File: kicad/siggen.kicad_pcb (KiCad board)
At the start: 4 copper layers, 39 x 60 mm, 100 parts, among them J1 Conn_Coaxial, J2 USB_C_Receptacle_USB2.0, Q1 BC857, Q2 BC847, Q3 BC857, U1 AD9954, U2 OPA859xDSG, U3 MCP2210x-SS, U4 AP62201-SOT563, U5 AP62201-SOT563, U6 TLV71x, U7 TLV71x, X1 ASE-xxxMHz, Y1 CSTNE12M0GH5L000R0

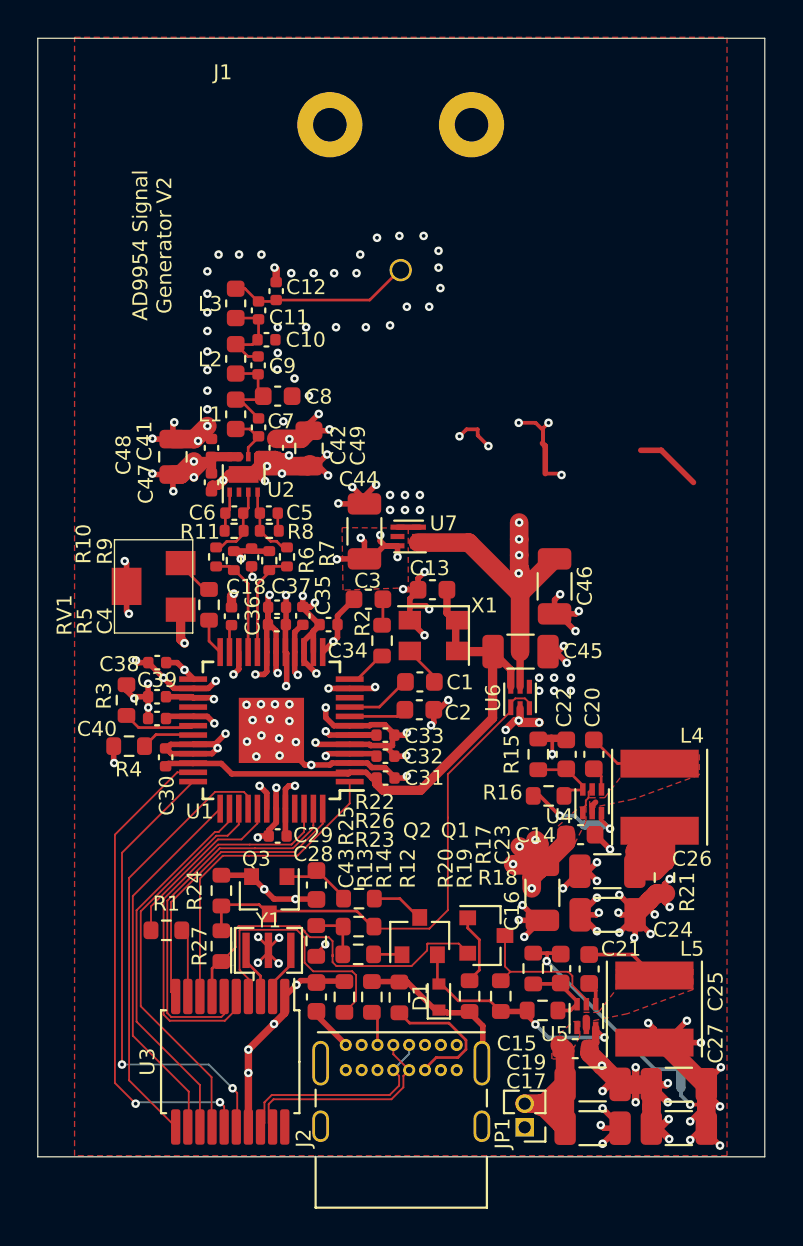
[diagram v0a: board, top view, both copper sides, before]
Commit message: Added output buffer; power LED
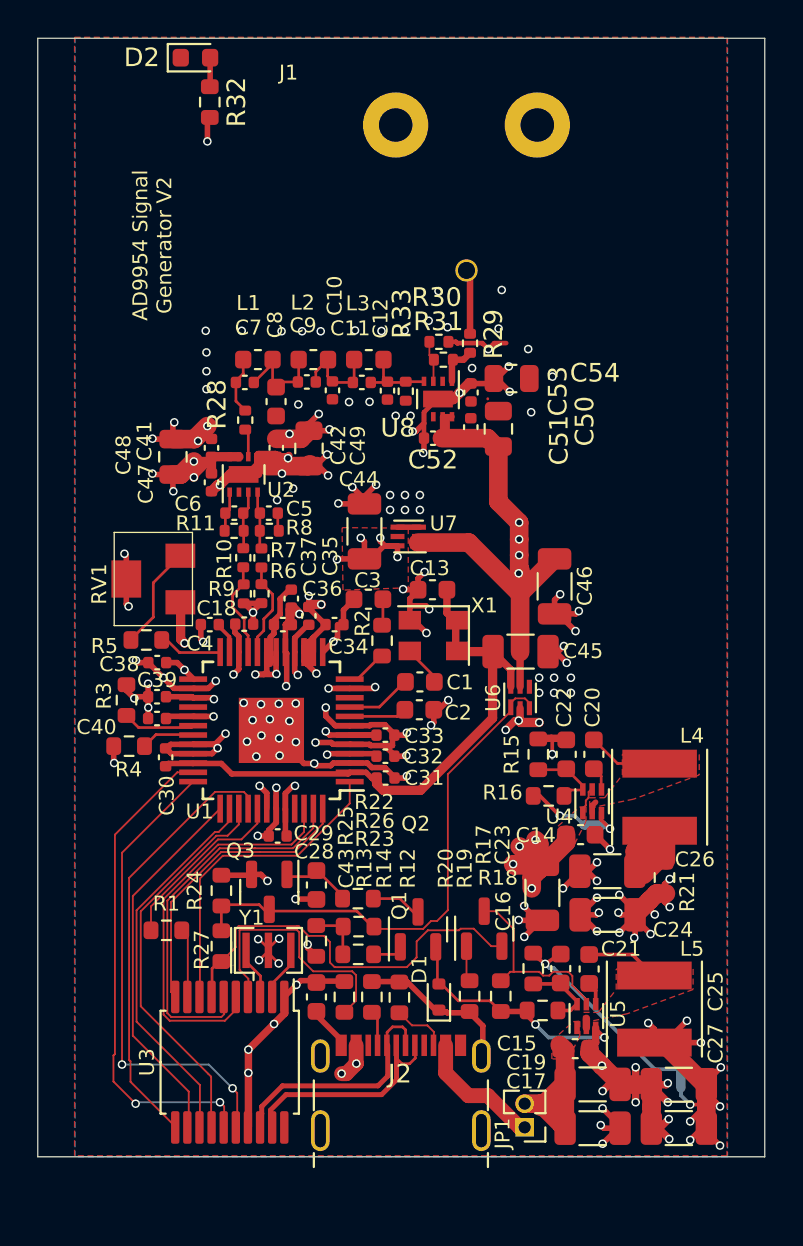
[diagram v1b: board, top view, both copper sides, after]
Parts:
- added C50: 1u, Capacitor_SMD:C_0805_2012Metric, F.Cu at (122.7, 121.0)
- added C51: 100n, Capacitor_SMD:C_0402_1005Metric, F.Cu at (121.2, 120.9)
- added C52: 100n, Capacitor_SMD:C_0402_1005Metric, F.Cu at (119.2, 121.5)
- added C53: 100n, Capacitor_SMD:C_0402_1005Metric, F.Cu at (121.2, 119.0)
- added C54: 1u, Capacitor_SMD:C_0805_2012Metric, F.Cu at (123.4, 118.2)
- added D2: LED, LED_SMD:LED_0603_1608Metric, F.Cu at (106.5, 101.0)
- added R28: 0, Resistor_SMD:R_0402_1005Metric, F.Cu at (109.1, 120.5)
- added R29: 0, Resistor_SMD:R_0402_1005Metric, F.Cu at (121.2, 116.4)
- added R30: 50, Resistor_SMD:R_0402_1005Metric, F.Cu at (119.5, 116.3)
- added R31: 50, Resistor_SMD:R_0402_1005Metric, F.Cu at (119.8, 117.2)
- added R32: 1k, Resistor_SMD:R_0603_1608Metric, F.Cu at (107.2, 103.4)
- added R33: 50, Resistor_SMD:R_0402_1005Metric, F.Cu at (117.7, 118.9)
- added U8: OPA859xDSG, Package_SON:WSON-8-1EP_2x2mm_P0.5mm_EP0.9x1.6mm, F.Cu at (119.5, 119.3)
- C5, C6: value 5.09p -> 7.3p
- J2: footprint proj_footprints:USB_C_Receptacle_GCT_USB4085_smaller_holes -> proj_footprints:USB_C_Receptacle_Molex_2171790001_16P_TopMnt_Horizontal
- R10, R7: value 142 -> 82
- R11, R8: value 220 -> 150
- R6, R9: value 120 -> 82
- moved C12 8.01 mm to (116.8, 118.9), turned to -90 degrees
- moved L3 7.75 mm to (115.8, 117.2), turned to 180 degrees
- moved C11 6.75 mm to (115.4, 118.5), turned to 180 degrees
- moved J2 4.74 mm to (117.5, 157.7)
- moved C10 4.46 mm to (113.8, 118.9), turned to -90 degrees
- moved L2 4.17 mm to (112.8, 117.2), turned to 180 degrees
- moved R5 3.86 mm to (103.8, 132.3), turned to 0 degrees
- moved C18 3.60 mm to (109.1, 131.4), turned to 0 degrees
- moved J1 3.53 mm to (121.0, 104.7)
- moved L1 3.17 mm to (109.8, 117.2), turned to 180 degrees
- moved C9 2.76 mm to (112.4, 118.4), turned to 180 degrees
- moved C7 2.52 mm to (109.1, 118.5), turned to 180 degrees
- moved R9 1.86 mm to (109.0, 129.8), turned to -90 degrees
- moved R6 1.82 mm to (110.0, 129.8), turned to -90 degrees
- moved R10 1.46 mm to (109.0, 127.9)
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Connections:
- C11 pad 1: /dds_analog/OUT_50 -> Net-(U8-+)
- C12 pad 1: /dds_analog/OUT_50 -> Net-(U8-+)
- J2 pad A8: Net-(J2-PadA8) -> unconnected-(J2-SBU1-PadA8)
- J2 pad B8: Net-(J2-PadB8) -> unconnected-(J2-SBU2-PadB8)
- L3 pad 1: /dds_analog/OUT_50 -> Net-(U8-+)
- U1 pad 10: Net-(U1-Pad10) -> unconnected-(U1-CRYSTAL_OUT-Pad10)
- U1 pad 28: Net-(U1-Pad28) -> unconnected-(U1-COMP_OUT-Pad28)
- U1 pad 45: Net-(U1-Pad45) -> unconnected-(U1-SYNC_CLK-Pad45)
- U2 pad 2: Net-(U2-Pad2) -> unconnected-(U2-NC-Pad2)
- U2 pad 6: Net-(C7-Pad2) -> Net-(R28-Pad1)
- U7 pad 5: Net-(U7-Pad5) -> unconnected-(U7-VOUT2-Pad5)
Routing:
- net +3V0: track 59.0 -> 108.3 mm, vias 9 -> 10
- net Net-(J2-VBUS-PadA4): track 0.00 -> 19.5 mm, vias 0 -> 2
- net -2V2: track 42.9 -> 51.1 mm, vias 18 -> 20
- net /dds_analog/OUT_50: track 9.83 -> 3.49 mm
- net GND: track 158.9 -> 152.9 mm, vias 143 -> 131
- net Net-(J2-CC2): track 7.34 -> 2.95 mm
- net Net-(U8-+): track 0.00 -> 4.14 mm
- net Net-(R5-Pad1): track 2.20 -> 5.66 mm
- net PWR_EN: track 19.3 -> 22.0 mm
- net Net-(Q1-C): track 8.06 -> 10.4 mm
- net Net-(U8--): track 0.00 -> 2.21 mm
- net Net-(U8-FB): track 0.00 -> 2.07 mm
- net Net-(Q1-B): track 3.86 -> 1.97 mm
- net +3V3: track 37.0 -> 35.2 mm
- net Net-(D2-A): track 0.00 -> 1.61 mm
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- added copper zone on B.Cu, net GND
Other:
- net class Default removed
- net class eurockt_diff100 removed
- net class eurockt_se50 removed
- net class jlc_diff100 removed
- net class jlc_se50 removed

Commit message: prepare for jlcpcb order (v2)
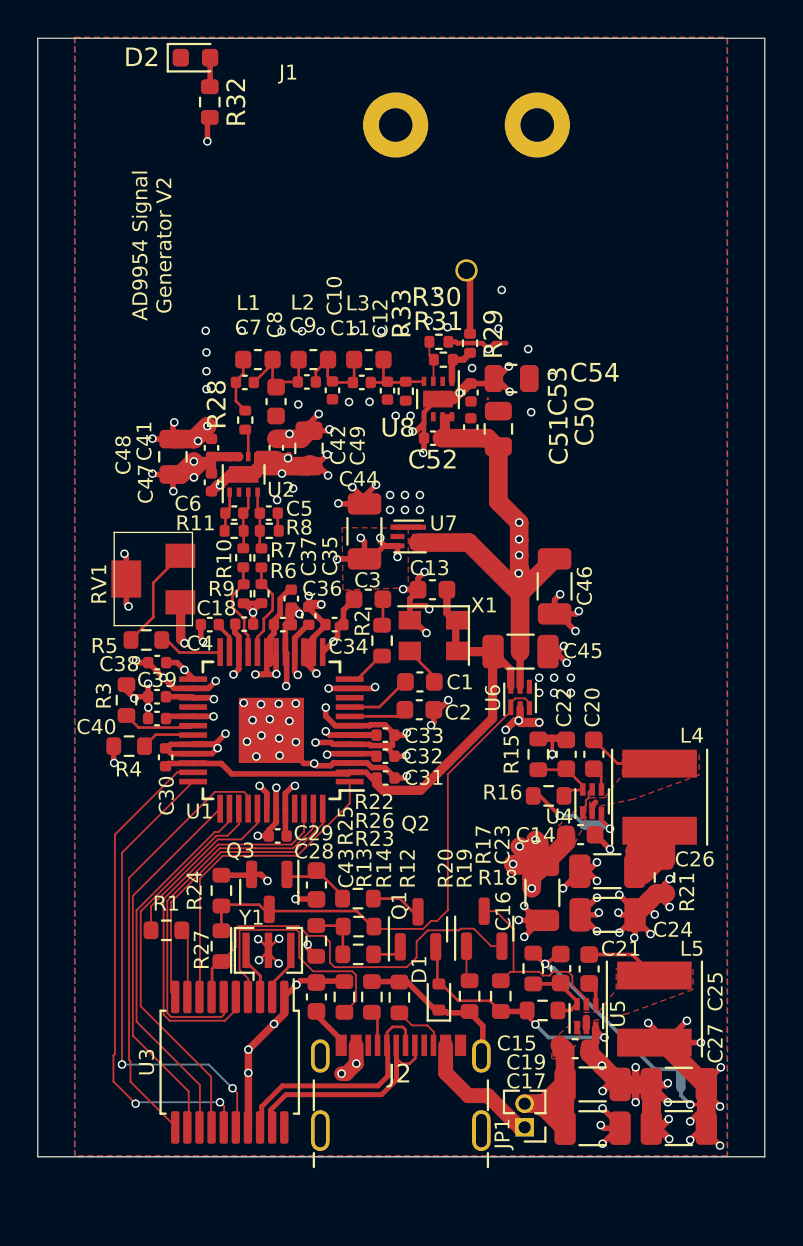
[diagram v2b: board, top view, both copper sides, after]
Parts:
- R30, R31: value 50 -> 150
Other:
- rule pad_to_mask_clearance: 0.048 -> 0
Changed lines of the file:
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@@
       (dielectric_constraints no)
     )
-    (pad_to_mask_clearance 0.048)
-    (solder_mask_min_width 0.102)
+    (pad_to_mask_clearance 0)
     (pcbplotparams
       (layerselection 0x00010fc_ffffffff)
@@
       (drillshape 0)
       (scaleselection 1)
-      (outputdirectory "grb")
+      (outputdirectory "grb-v2")
     )
   )
@@
     (fp_line (start 1.6 0.8) (end -1.6 0.8)
       (stroke (width 0.1) (type solid)) (layer "F.Fab"))
-    (pad "1" smd roundrect (at -1.475 0 90) (size 1.15 1.8) (layers "F.Cu" "F.Paste" "F.Mask") (roundrect_rratio 0.217391)
+    (pad "1" smd roundrect (at -1.475 0 90) (size 1.15 1.8) (layers "F.Cu" "F.Paste" "F.Mask") (roundrect_rratio 0.2173913043)
       (net 3 "GND") (pintype "passive"))
-    (pad "2" smd roundrect (at 1.475 0 90) (size 1.15 1.8) (layers "F.Cu" "F.Paste" "F.Mask") (roundrect_rratio 0.217391)
+    (pad "2" smd roundrect (at 1.475 0 90) (size 1.15 1.8) (layers "F.Cu" "F.Paste" "F.Mask") (roundrect_rratio 0.2173913043)
       (net 15 "VBUS") (pintype "passive"))
     (model "${KICAD6_3DMODEL_DIR}/Capacitor_SMD.3dshapes/C_1206_3216Metric.wrl"
@@
     (fp_line (start 1.6 0.8) (end -1.6 0.8)
       (stroke (width 0.1) (type solid)) (layer "F.Fab"))
-    (pad "1" smd roundrect (at -1.475 0 180) (size 1.15 1.8) (layers "F.Cu" "F.Paste" "F.Mask") (roundrect_rratio 0.217391)
+    (pad "1" smd roundrect (at -1.475 0 180) (size 1.15 1.8) (layers "F.Cu" "F.Paste" "F.Mask") (roundrect_rratio 0.2173913043)
       (net 3 "GND") (pintype "passive"))
-    (pad "2" smd roundrect (at 1.475 0 180) (size 1.15 1.8) (layers "F.Cu" "F.Paste" "F.Mask") (roundrect_rratio 0.217391)
+    (pad "2" smd roundrect (at 1.475 0 180) (size 1.15 1.8) (layers "F.Cu" "F.Paste" "F.Mask") (roundrect_rratio 0.2173913043)
       (net 15 "VBUS") (pintype "passive"))
     (model "${KICAD6_3DMODEL_DIR}/Capacitor_SMD.3dshapes/C_1206_3216Metric.wrl"
@@
     (fp_line (start 1.6 0.8) (end -1.6 0.8)
       (stroke (width 0.1) (type solid)) (layer "F.Fab"))
-    (pad "1" smd roundrect (at -1.475 0 180) (size 1.15 1.8) (layers "F.Cu" "F.Paste" "F.Mask") (roundrect_rratio 0.217391)
+    (pad "1" smd roundrect (at -1.475 0 180) (size 1.15 1.8) (layers "F.Cu" "F.Paste" "F.Mask") (roundrect_rratio 0.2173913043)
       (net 16 "-2V2") (pintype "passive"))
-    (pad "2" smd roundrect (at 1.475 0 180) (size 1.15 1.8) (layers "F.Cu" "F.Paste" "F.Mask") (roundrect_rratio 0.217391)
+    (pad "2" smd roundrect (at 1.475 0 180) (size 1.15 1.8) (layers "F.Cu" "F.Paste" "F.Mask") (roundrect_rratio 0.2173913043)
       (net 15 "VBUS") (pintype "passive"))
     (model "${KICAD6_3DMODEL_DIR}/Capacitor_SMD.3dshapes/C_1206_3216Metric.wrl"
@@
     (fp_line (start 1.6 0.8) (end -1.6 0.8)
       (stroke (width 0.1) (type solid)) (layer "F.Fab"))
-    (pad "1" smd roundrect (at -1.475 0 180) (size 1.15 1.8) (layers "F.Cu" "F.Paste" "F.Mask") (roundrect_rratio 0.217391)
+    (pad "1" smd roundrect (at -1.475 0 180) (size 1.15 1.8) (layers "F.Cu" "F.Paste" "F.Mask") (roundrect_rratio 0.2173913043)
       (net 22 "+3V3") (pintype "passive"))
-    (pad "2" smd roundrect (at 1.475 0 180) (size 1.15 1.8) (layers "F.Cu" "F.Paste" "F.Mask") (roundrect_rratio 0.217391)
+    (pad "2" smd roundrect (at 1.475 0 180) (size 1.15 1.8) (layers "F.Cu" "F.Paste" "F.Mask") (roundrect_rratio 0.2173913043)
       (net 3 "GND") (pintype "passive"))
     (model "${KICAD6_3DMODEL_DIR}/Capacitor_SMD.3dshapes/C_1206_3216Metric.wrl"
@@
     (fp_line (start 1.6 0.8) (end -1.6 0.8)
       (stroke (width 0.1) (type solid)) (layer "F.Fab"))
-    (pad "1" smd roundrect (at -1.475 0 180) (size 1.15 1.8) (layers "F.Cu" "F.Paste" "F.Mask") (roundrect_rratio 0.217391)
+    (pad "1" smd roundrect (at -1.475 0 180) (size 1.15 1.8) (layers "F.Cu" "F.Paste" "F.Mask") (roundrect_rratio 0.2173913043)
       (net 3 "GND") (pintype "passive"))
-    (pad "2" smd roundrect (at 1.475 0 180) (size 1.15 1.8) (layers "F.Cu" "F.Paste" "F.Mask") (roundrect_rratio 0.217391)
+    (pad "2" smd roundrect (at 1.475 0 180) (size 1.15 1.8) (layers "F.Cu" "F.Paste" "F.Mask") (roundrect_rratio 0.2173913043)
       (net 16 "-2V2") (pintype "passive"))
     (model "${KICAD6_3DMODEL_DIR}/Capacitor_SMD.3dshapes/C_1206_3216Metric.wrl"
@@
     (fp_line (start 1.6 0.8) (end -1.6 0.8)
       (stroke (width 0.1) (type solid)) (layer "F.Fab"))
-    (pad "1" smd roundrect (at -1.475 0 180) (size 1.15 1.8) (layers "F.Cu" "F.Paste" "F.Mask") (roundrect_rratio 0.217391)
+    (pad "1" smd roundrect (at -1.475 0 180) (size 1.15 1.8) (layers "F.Cu" "F.Paste" "F.Mask") (roundrect_rratio 0.2173913043)
       (net 24 "Net-(C26-Pad1)") (pintype "passive"))
-    (pad "2" smd roundrect (at 1.475 0 180) (size 1.15 1.8) (layers "F.Cu" "F.Paste" "F.Mask") (roundrect_rratio 0.217391)
+    (pad "2" smd roundrect (at 1.475 0 180) (size 1.15 1.8) (layers "F.Cu" "F.Paste" "F.Mask") (roundrect_rratio 0.2173913043)
       (net 3 "GND") (pintype "passive"))
     (model "${KICAD6_3DMODEL_DIR}/Capacitor_SMD.3dshapes/C_1206_3216Metric.wrl"
@@
     (fp_line (start 1.6 0.8) (end -1.6 0.8)
       (stroke (width 0.1) (type solid)) (layer "F.Fab"))
-    (pad "1" smd roundrect (at -1.475 0 180) (size 1.15 1.8) (layers "F.Cu" "F.Paste" "F.Mask") (roundrect_rratio 0.217391)
+    (pad "1" smd roundrect (at -1.475 0 180) (size 1.15 1.8) (layers "F.Cu" "F.Paste" "F.Mask") (roundrect_rratio 0.2173913043)
       (net 3 "GND") (pintype "passive"))
-    (pad "2" smd roundrect (at 1.475 0 180) (size 1.15 1.8) (layers "F.Cu" "F.Paste" "F.Mask") (roundrect_rratio 0.217391)
+    (pad "2" smd roundrect (at 1.475 0 180) (size 1.15 1.8) (layers "F.Cu" "F.Paste" "F.Mask") (roundrect_rratio 0.2173913043)
       (net 16 "-2V2") (pintype "passive"))
     (model "${KICAD6_3DMODEL_DIR}/Capacitor_SMD.3dshapes/C_1206_3216Metric.wrl"
@@
     (fp_line (start 1.6 0.8) (end -1.6 0.8)
       (stroke (width 0.1) (type solid)) (layer "F.Fab"))
-    (pad "1" smd roundrect (at -1.475 0 180) (size 1.15 1.8) (layers "F.Cu" "F.Paste" "F.Mask") (roundrect_rratio 0.217391)
+    (pad "1" smd roundrect (at -1.475 0 180) (size 1.15 1.8) (layers "F.Cu" "F.Paste" "F.Mask") (roundrect_rratio 0.2173913043)
       (net 3 "GND") (pintype "passive"))
-    (pad "2" smd roundrect (at 1.475 0 180) (size 1.15 1.8) (layers "F.Cu" "F.Paste" "F.Mask") (roundrect_rratio 0.217391)
+    (pad "2" smd roundrect (at 1.475 0 180) (size 1.15 1.8) (layers "F.Cu" "F.Paste" "F.Mask") (roundrect_rratio 0.2173913043)
       (net 14 "+1V8") (pintype "passive"))
     (model "${KICAD6_3DMODEL_DIR}/Capacitor_SMD.3dshapes/C_1206_3216Metric.wrl"
@@
     (fp_line (start 1.6 0.8) (end -1.6 0.8)
       (stroke (width 0.1) (type solid)) (layer "F.Fab"))
-    (pad "1" smd roundrect (at -1.475 0 90) (size 1.15 1.8) (layers "F.Cu" "F.Paste" "F.Mask") (roundrect_rratio 0.217391)
+    (pad "1" smd roundrect (at -1.475 0 90) (size 1.15 1.8) (layers "F.Cu" "F.Paste" "F.Mask") (roundrect_rratio 0.2173913043)
       (net 3 "GND") (pintype "passive"))
-    (pad "2" smd roundrect (at 1.475 0 90) (size 1.15 1.8) (layers "F.Cu" "F.Paste" "F.Mask") (roundrect_rratio 0.217391)
+    (pad "2" smd roundrect (at 1.475 0 90) (size 1.15 1.8) (layers "F.Cu" "F.Paste" "F.Mask") (roundrect_rratio 0.2173913043)
       (net 26 "+3V0") (pintype "passive"))
     (model "${KICAD6_3DMODEL_DIR}/Capacitor_SMD.3dshapes/C_1206_3216Metric.wrl"
@@
     (fp_line (start 1.6 0.8) (end -1.6 0.8)
       (stroke (width 0.1) (type solid)) (layer "F.Fab"))
-    (pad "1" smd roundrect (at -1.475 0 270) (size 1.15 1.8) (layers "F.Cu" "F.Paste" "F.Mask") (roundrect_rratio 0.217391)
+    (pad "1" smd roundrect (at -1.475 0 270) (size 1.15 1.8) (layers "F.Cu" "F.Paste" "F.Mask") (roundrect_rratio 0.2173913043)
       (net 3 "GND") (pintype "passive"))
-    (pad "2" smd roundrect (at 1.475 0 270) (size 1.15 1.8) (layers "F.Cu" "F.Paste" "F.Mask") (roundrect_rratio 0.217391)
+    (pad "2" smd roundrect (at 1.475 0 270) (size 1.15 1.8) (layers "F.Cu" "F.Paste" "F.Mask") (roundrect_rratio 0.2173913043)
       (net 6 "+1V8_analog") (pintype "passive"))
     (model "${KICAD6_3DMODEL_DIR}/Capacitor_SMD.3dshapes/C_1206_3216Metric.wrl"
@@
         (effects (font (size 1 1) (thickness 0.15)))
     )
-    (fp_text value "50" (at 0 1.17) (layer "F.Fab")
+    (fp_text value "150" (at 0 1.17) (layer "F.Fab")
         (effects (font (size 1 1) (thickness 0.15)))
     )
@@
         (effects (font (size 1 1) (thickness 0.15)))
     )
-    (fp_text value "50" (at 0 1.17) (layer "F.Fab")
+    (fp_text value "150" (at 0 1.17) (layer "F.Fab")
         (effects (font (size 1 1) (thickness 0.15)))
     )

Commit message: modified a few values (as loaded on v2 prototype board)
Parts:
- R17: value 21.5k -> 31.6k
- R18: value 12.1k -> 18k
- R31: value 150 -> 50
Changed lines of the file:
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@@
         (effects (font (size 0.8 0.8) (thickness 0.153)))
     )
-    (fp_text value "21.5k" (at 0 1.43 90) (layer "F.Fab")
+    (fp_text value "31.6k" (at 0 1.43 90) (layer "F.Fab")
         (effects (font (size 1 1) (thickness 0.15)))
     )
@@
         (effects (font (size 0.8 0.8) (thickness 0.153)))
     )
-    (fp_text value "12.1k" (at 0 1.43) (layer "F.Fab")
+    (fp_text value "18k" (at 0 1.43) (layer "F.Fab")
         (effects (font (size 1 1) (thickness 0.15)))
     )
@@
         (effects (font (size 1 1) (thickness 0.15)))
     )
-    (fp_text value "150" (at 0 1.17) (layer "F.Fab")
-        (effects (font (size 1 1) (thickness 0.15)))
-    )
+    (fp_text value "50" (at 0 1.17) (layer "F.Fab")
+        (effects (font (size 1 1) (thickness 0.15)))
+    )

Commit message: changed values in schematic for v2 board
Most notably: moved from +3.0/-2.2V to +2.8/-2.4V analog supply.
This required changing the diff-amp resistors to stay within
the common-mode range of the AD9954 and the OPA859.
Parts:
- D1: value D -> BAT54XV2T1G
- R1, R5: value 3k5 -> 3k3
- R10, R7: value 82 -> 120
- R17: value 31.6k -> 24k
- R18: value 18k -> 12k
- R21: value 0.1 -> 0
- R30: value 150 -> 232
- R31: value 50 -> 150
- U6, U7: value TLV71x -> TLV7101828
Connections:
- net +3V0 renamed +2V8
- net -2V2 renamed -2V4
